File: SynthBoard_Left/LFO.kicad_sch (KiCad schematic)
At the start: 17 parts, among them Q2 2SC1623(RANGE:300-400), U1 TJM4558CDT

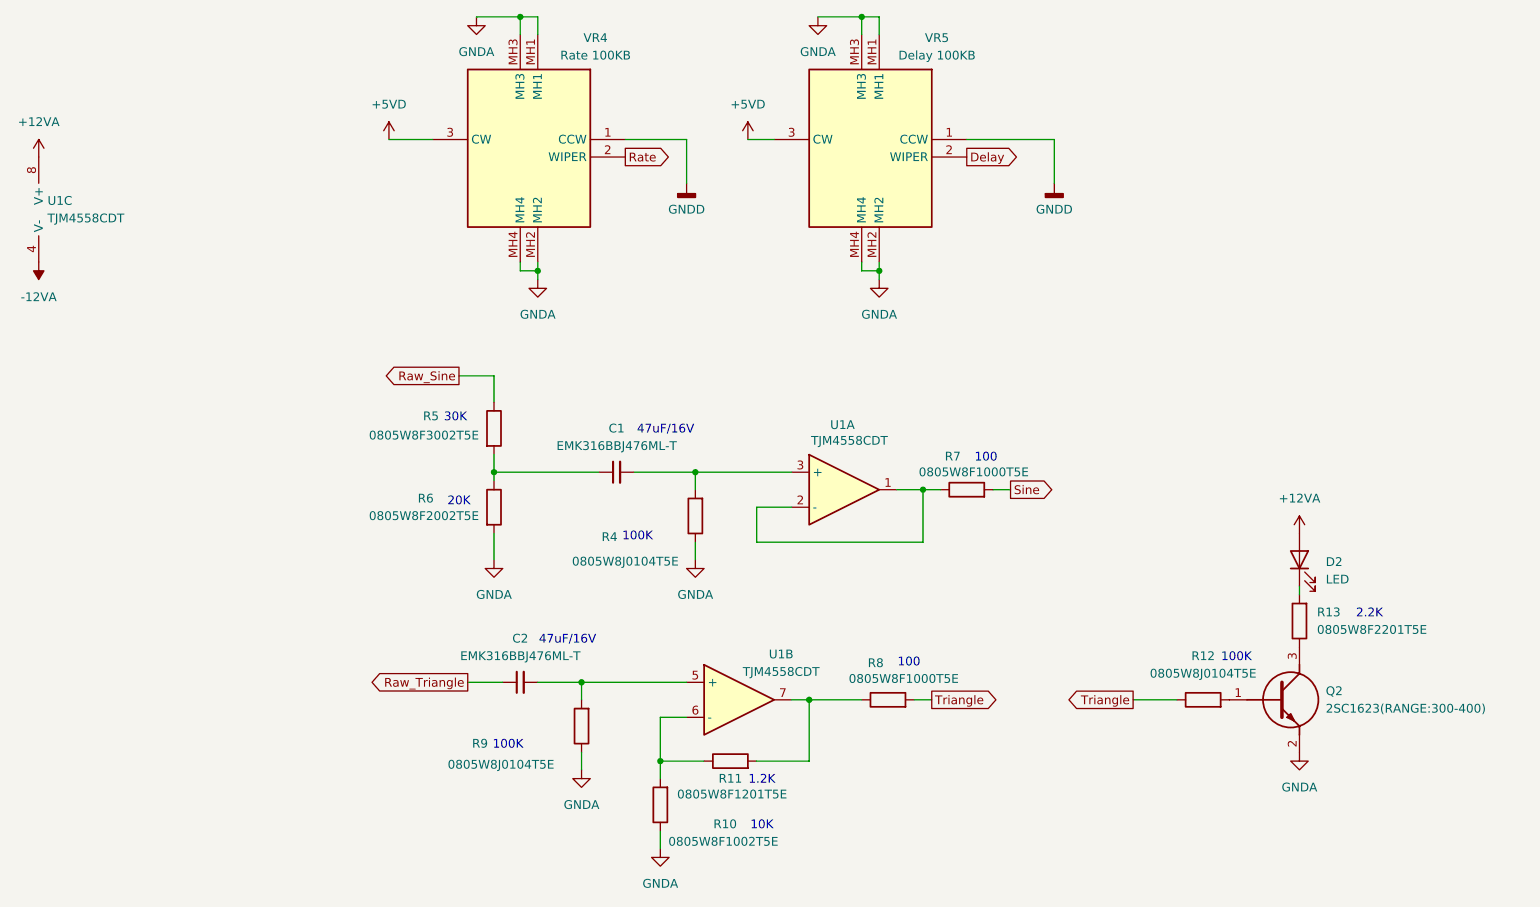
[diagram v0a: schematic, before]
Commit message: SynthBoard_Left
JLCPCBでBasic部品に置き換えた
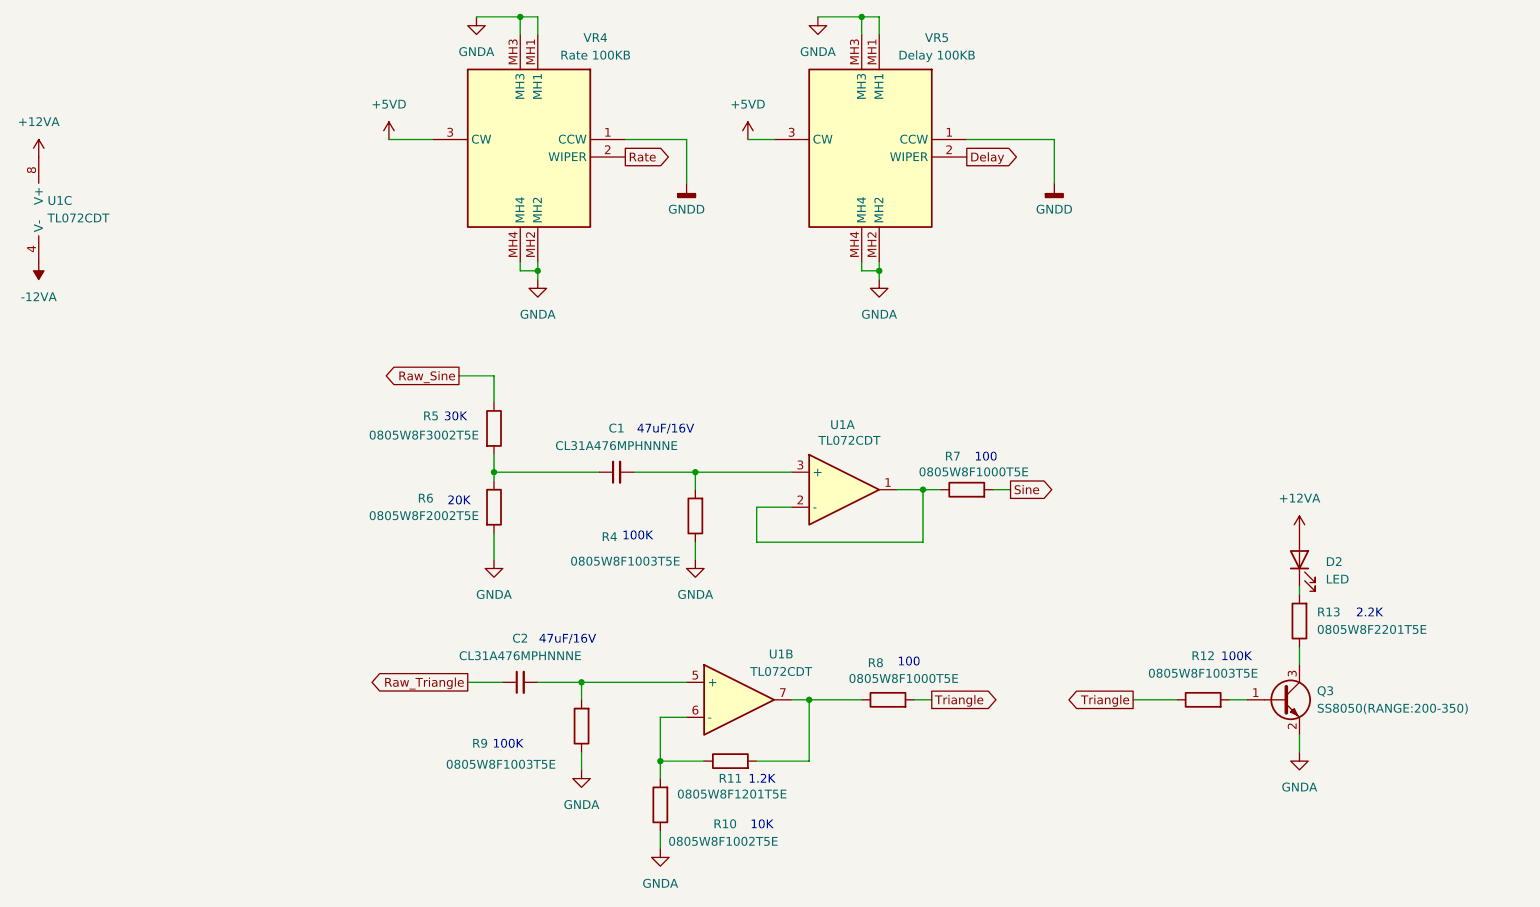
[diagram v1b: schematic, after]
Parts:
- removed Q2: 2SC1623(RANGE:300-400), SamacSys_parts:SOT95P237X125-3N, symbol SamacSys_Parts:2SC1623-A
- added Q3: SS8050(RANGE:200-350), SamacSys_parts:SOT95P240X115-3N, symbol Transistor_BJT:SS8050
- C1, C2: value EMK316BBJ476ML-T -> CL31A476MPHNNNE
- R12, R4, R9: value 0805W8J0104T5E -> 0805W8F1003T5E
- U1: value TJM4558CDT -> TL072CDT
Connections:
- net GNDA: now also Q3.2 (E)
- net at R13.1: now also Q3.3 (C)
- net at R12.2: now also Q3.1 (B)
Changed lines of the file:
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@@
+	(wire
+		(pts
+			(xy 229.87 124.46) (xy 229.87 127)
+		)
+		(stroke
+			(width 0)
+			(type default)
+		)
+	)
 	(wire
 		(pts
@@
 	(wire
 		(pts
+			(xy 229.87 137.16) (xy 229.87 139.7)
+		)
+		(stroke
+			(width 0)
+			(type default)
+		)
+	)
+	(wire
+		(pts
 			(xy 107.95 85.09) (xy 113.03 85.09)
 		)
@@
 		(pts
 			(xy 142.24 99.06) (xy 156.21 99.06)
+		)
+		(stroke
+			(width 0)
+			(type default)
+		)
+	)
+	(wire
+		(pts
+			(xy 219.71 132.08) (xy 222.25 132.08)
 		)
 		(stroke
@@
 	)
 	(symbol
+		(lib_id "Transistor_BJT:SS8050")
+		(at 227.33 132.08 0)
+		(unit 1)
+		(exclude_from_sim no)
+		(in_bom yes)
+		(on_board yes)
+		(dnp no)
+		(fields_autoplaced yes)
+		(property "Reference" "Q3"
+			(at 232.41 130.8099 0)
+			(effects
+				(font
+					(size 1.27 1.27)
+				)
+				(justify left)
+			)
+		)
+		(property "Value" "SS8050(RANGE:200-350)"
+			(at 232.41 133.3499 0)
+			(effects
+				(font
+					(size 1.27 1.27)
+				)
+				(justify left)
+			)
+		)
+		(property "Footprint" "SamacSys_parts:SOT95P240X115-3N"
+			(at 232.41 139.446 0)
+			(effects
+				(font
+					(size 1.27 1.27)
+					(italic yes)
+				)
+				(justify left)
+				(hide yes)
+			)
+		)
+		(property "Datasheet" "http://www.secosgmbh.com/datasheet/products/SSMPTransistor/SOT-23/SS8050.pdf"
+			(at 232.41 136.906 0)
+			(effects
+				(font
+					(size 1.27 1.27)
+				)
+				(justify left)
+				(hide yes)
+			)
+		)
+		(property "Description" "General Purpose NPN Transistor, 1.5A Ic, 25V Vce, SOT-23"
+			(at 261.366 134.366 0)
+			(effects
+				(font
+					(size 1.27 1.27)
+				)
+				(hide yes)
+			)
+		)
+		(pin "1"
+		)
+		(pin "2"
+		)
+		(pin "3"
+		)
+		(instances
+			(project "SynthBoard"
+				(path "/92765e2f-a998-485f-b610-76a9d5b50cba/703aad3c-b177-4856-b861-e207f207807c"
+					(reference "Q3")
+					(unit 1)
+				)
+			)
+		)
+	)
+	(symbol
 		(lib_id "power:GNDD")
 		(at 194.31 57.15 0)
@@
 			)
 		)
-		(property "Value" "TJM4558CDT"
+		(property "Value" "TL072CDT"
 			(at 164.592 94.488 0)
 			(effects
@@
 			)
 		)
-		(property "Value" "TJM4558CDT"
+		(property "Value" "TL072CDT"
 			(at 154.686 128.016 0)
 			(effects
@@
 			)
 		)
-		(property "Value" "0805W8J0104T5E"
+		(property "Value" "0805W8F1003T5E"
 			(at 114.046 141.478 0)
 			(effects
@@
 			)
 		)
-		(property "Value" "0805W8J0104T5E"
+		(property "Value" "0805W8F1003T5E"
 			(at 132.08 112.014 0)
 			(effects
@@
 			)
 		)
-		(property "Value" "TJM4558CDT"
+		(property "Value" "TL072CDT"
 			(at 48.26 62.2299 0)
 			(effects
@@
 			)
 		)
-		(property "Value" "EMK316BBJ476ML-T"
+		(property "Value" "CL31A476MPHNNNE"
 			(at 116.8463 125.73 90)
 			(effects
@@
 				(path "/92765e2f-a998-485f-b610-76a9d5b50cba/703aad3c-b177-4856-b861-e207f207807c"
 					(reference "C2")
-					(unit 1)
-				)
-			)
-		)
-	)
-	(symbol
-		(lib_id "SamacSys_Parts:2SC1623-A")
-		(at 219.71 132.08 0)
-		(unit 1)
-		(exclude_from_sim no)
-		(in_bom yes)
-		(on_board yes)
-		(dnp no)
-		(fields_autoplaced yes)
-		(property "Reference" "Q2"
-			(at 233.68 130.8099 0)
-			(effects
-				(font
-					(size 1.27 1.27)
-				)
-				(justify left)
-			)
-		)
-		(property "Value" "2SC1623(RANGE:300-400)"
-			(at 233.68 133.3499 0)
-			(effects
-				(font
-					(size 1.27 1.27)
-				)
-				(justify left)
-			)
-		)
-		(property "Footprint" "SamacSys_parts:SOT95P237X125-3N"
-			(at 233.68 233.35 0)
-			(effects
-				(font
-					(size 1.27 1.27)
-				)
-				(justify left top)
-				(hide yes)
-			)
-		)
-		(property "Datasheet" "https://www.mouser.in/datasheet/2/258/2SC1623_SOT_23_-1625845.pdf"
-			(at 233.68 333.35 0)
-			(effects
-				(font
-					(size 1.27 1.27)
-				)
-				(justify left top)
-				(hide yes)
-			)
-		)
-		(property "Description" "Renesas Electronics 2SC1623-A NPN Bipolar Transistor, 100 mA, 50 V, 3-Pin MiniMold"
-			(at 219.71 132.08 0)
-			(effects
-				(font
-					(size 1.27 1.27)
-				)
-				(hide yes)
-			)
-		)
-		(property "Height" "1.25"
-			(at 233.68 533.35 0)
-			(effects
-				(font
-					(size 1.27 1.27)
-				)
-				(justify left top)
-				(hide yes)
-			)
-		)
-		(property "Manufacturer_Name" "Renesas Electronics"
-			(at 233.68 633.35 0)
-			(effects
-				(font
-					(size 1.27 1.27)
-				)
-				(justify left top)
-				(hide yes)
-			)
-		)
-		(property "Manufacturer_Part_Number" "2SC1623-A"
-			(at 233.68 733.35 0)
-			(effects
-				(font
-					(size 1.27 1.27)
-				)
-				(justify left top)
-				(hide yes)
-			)
-		)
-		(property "Mouser Part Number" ""
-			(at 233.68 833.35 0)
-			(effects
-				(font
-					(size 1.27 1.27)
-				)
-				(justify left top)
-				(hide yes)
-			)
-		)
-		(property "Mouser Price/Stock" ""
-			(at 233.68 933.35 0)
-			(effects
-				(font
-					(size 1.27 1.27)
-				)
-				(justify left top)
-				(hide yes)
-			)
-		)
-		(property "Arrow Part Number" ""
-			(at 233.68 1033.35 0)
-			(effects
-				(font
-					(size 1.27 1.27)
-				)
-				(justify left top)
-				(hide yes)
-			)
-		)
-		(property "Arrow Price/Stock" ""
-			(at 233.68 1133.35 0)
-			(effects
-				(font
-					(size 1.27 1.27)
-				)
-				(justify left top)
-				(hide yes)
-			)
-		)
-		(pin "3"
-		)
-		(pin "2"
-		)
-		(pin "1"
-		)
-		(instances
-			(project ""
-				(path "/92765e2f-a998-485f-b610-76a9d5b50cba/703aad3c-b177-4856-b861-e207f207807c"
-					(reference "Q2")
 					(unit 1)
 				)
@@
 			)
 		)
-		(property "Value" "0805W8J0104T5E"
+		(property "Value" "0805W8F1003T5E"
 			(at 215.9 128.27 90)
 			(effects
@@
 			)
 		)
-		(property "Value" "EMK316BBJ476ML-T"
+		(property "Value" "CL31A476MPHNNNE"
 			(at 130.8163 95.25 90)
 			(effects
